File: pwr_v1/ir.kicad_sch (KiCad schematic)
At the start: 1 part

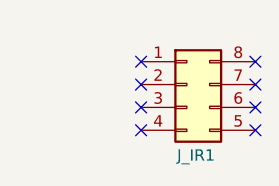
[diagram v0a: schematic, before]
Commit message: Sch and Layout updated; Added batt sup ckt, placed and routed all motor drivers.
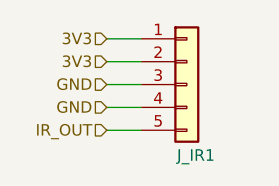
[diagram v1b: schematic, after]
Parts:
- J_IR1: value Conn_02x04_Counter_Clockwise -> Connector_Generic:Conn_01x05; symbol Connector_Generic:Conn_02x04_Counter_Clockwise -> Connector_Generic:Conn_01x05
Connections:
- net 3V3: now reaches J_IR1.1 (Pin_1)
- net 3V3: now also J_IR1.2 (Pin_2)
- net GND: now reaches J_IR1.3 (Pin_3)
- net GND: now also J_IR1.4 (Pin_4)
- net IR_OUT: now reaches J_IR1.5 (Pin_5)
- no-connect marks 8 -> 0
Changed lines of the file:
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@@
 	(generator_version "8.0")
 	(paper "A5")
-	(no_connect
-		(at 92.71 66.04)
+	(wire
+		(pts
+			(xy 88.9 60.96) (xy 92.71 60.96)
+		)
+		(stroke
+			(width 0)
+			(type default)
+		)
 	)
-	(no_connect
-		(at 105.41 58.42)
+	(wire
+		(pts
+			(xy 88.9 63.5) (xy 92.71 63.5)
+		)
+		(stroke
+			(width 0)
+			(type default)
+		)
 	)
-	(no_connect
-		(at 105.41 66.04)
+	(wire
+		(pts
+			(xy 88.9 58.42) (xy 92.71 58.42)
+		)
+		(stroke
+			(width 0)
+			(type default)
+		)
 	)
-	(no_connect
-		(at 92.71 58.42)
+	(wire
+		(pts
+			(xy 88.9 66.04) (xy 92.71 66.04)
+		)
+		(stroke
+			(width 0)
+			(type default)
+		)
 	)
-	(no_connect
-		(at 105.41 63.5)
+	(wire
+		(pts
+			(xy 88.9 55.88) (xy 92.71 55.88)
+		)
+		(stroke
+			(width 0)
+			(type default)
+		)
 	)
-	(no_connect
-		(at 92.71 63.5)
+	(hierarchical_label "GND"
+		(shape input)
+		(at 88.9 63.5 180)
+		(fields_autoplaced yes)
+		(effects
+			(font
+				(size 1.27 1.27)
+			)
+			(justify right)
+		)
 	)
-	(no_connect
-		(at 92.71 60.96)
+	(hierarchical_label "3V3"
+		(shape input)
+		(at 88.9 55.88 180)
+		(fields_autoplaced yes)
+		(effects
+			(font
+				(size 1.27 1.27)
+			)
+			(justify right)
+		)
 	)
-	(no_connect
-		(at 105.41 60.96)
+	(hierarchical_label "IR_OUT"
+		(shape input)
+		(at 88.9 66.04 180)
+		(fields_autoplaced yes)
+		(effects
+			(font
+				(size 1.27 1.27)
+			)
+			(justify right)
+		)
+	)
+	(hierarchical_label "3V3"
+		(shape input)
+		(at 88.9 58.42 180)
+		(fields_autoplaced yes)
+		(effects
+			(font
+				(size 1.27 1.27)
+			)
+			(justify right)
+		)
+	)
+	(hierarchical_label "GND"
+		(shape input)
+		(at 88.9 60.96 180)
+		(fields_autoplaced yes)
+		(effects
+			(font
+				(size 1.27 1.27)
+			)
+			(justify right)
+		)
 	)
 	(symbol
-		(lib_id "Connector_Generic:Conn_02x04_Counter_Clockwise")
+		(lib_id "Connector_Generic:Conn_01x05")
 		(at 97.79 60.96 0)
 		(unit 1)
@@
 			)
 		)
-		(property "Value" "Conn_02x04_Counter_Clockwise"
+		(property "Value" "Connector_Generic:Conn_01x05"
 			(at 99.06 54.61 0)
 			(effects
@@
 			)
 		)
-		(property "Description" "Generic connector, double row, 02x04, counter clockwise pin numbering scheme (similar to DIP package numbering), script generated (kicad-library-utils/schlib/autogen/connector/)"
+		(property "Description" "Generic connector, single row, 01x05, script generated (kicad-library-utils/schlib/autogen/connector/)"
 			(at 97.79 60.96 0)
 			(effects
@@
 		(pin "3"
 		)
-		(pin "6"
-		)
 		(pin "4"
 		)
@@
 		(pin "1"
 		)
-		(pin "7"
-		)
-		(pin "8"
-		)
 		(instances

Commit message: Schematic and layout updated; Motor driver alignments and planes;  Few components updated
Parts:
- J_IR1: footprint (none) -> Connector_PinHeader_2.54mm:PinHeader_1x05_P2.54mm_Vertical
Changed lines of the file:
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@@
 			)
 		)
-		(property "Footprint" ""
+		(property "Footprint" "Connector_PinHeader_2.54mm:PinHeader_1x05_P2.54mm_Vertical"
 			(at 97.79 60.96 0)
 			(effects
@@
 			)
 		)
-		(property "Description" "Generic connector, single row, 01x05, script generated (kicad-library-utils/schlib/autogen/connector/)"
+		(property "Description" ""
 			(at 97.79 60.96 0)
 			(effects

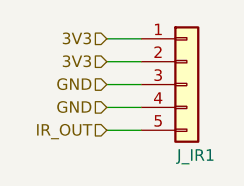
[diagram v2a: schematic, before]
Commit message: Schematic updated; Layout updated; STM PinMappings file added
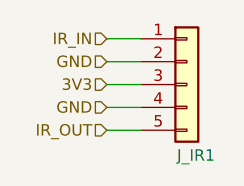
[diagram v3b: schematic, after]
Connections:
- net 3V3: now also J_IR1.3 (Pin_3); no longer J_IR1.1 (Pin_1), J_IR1.2 (Pin_2)
- net GND: now also J_IR1.2 (Pin_2); no longer J_IR1.3 (Pin_3)
- new net IR_IN: J_IR1.1 (Pin_1)
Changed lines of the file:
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@@
 		)
 	)
-	(hierarchical_label "3V3"
+	(hierarchical_label "IR_IN"
 		(shape input)
 		(at 88.9 55.88 180)
@@
 		)
 	)
-	(hierarchical_label "3V3"
+	(hierarchical_label "GND"
 		(shape input)
 		(at 88.9 58.42 180)
@@
 		)
 	)
-	(hierarchical_label "GND"
+	(hierarchical_label "3V3"
 		(shape input)
 		(at 88.9 60.96 180)

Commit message: Schematic and layout updated; Layout placement and routing completed
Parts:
- J_IR1: footprint Connector_PinHeader_2.54mm:PinHeader_1x05_P2.54mm_Vertical -> Connector_PinHeader_2.54mm:PinHeader_1x05_P2.54mm_Vertical_SMD_Pin1Left
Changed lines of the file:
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@@
 			)
 		)
-		(property "Footprint" "Connector_PinHeader_2.54mm:PinHeader_1x05_P2.54mm_Vertical"
+		(property "Footprint" "Connector_PinHeader_2.54mm:PinHeader_1x05_P2.54mm_Vertical_SMD_Pin1Left"
 			(at 97.79 60.96 0)
 			(effects

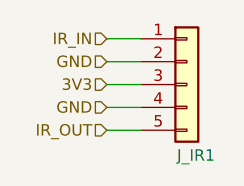
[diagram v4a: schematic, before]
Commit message: Sch: DNP updated, JLC part numbers updated for all components; Lay: Fiducial placement, routing aligned.
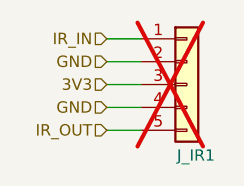
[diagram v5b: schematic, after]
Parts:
- J_IR1: now not fitted; now left out of the parts list
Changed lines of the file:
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@@
 		(unit 1)
 		(exclude_from_sim no)
-		(in_bom yes)
+		(in_bom no)
 		(on_board yes)
-		(dnp no)
+		(dnp yes)
 		(property "Reference" "J_IR1"
 			(at 98.806 68.834 0)

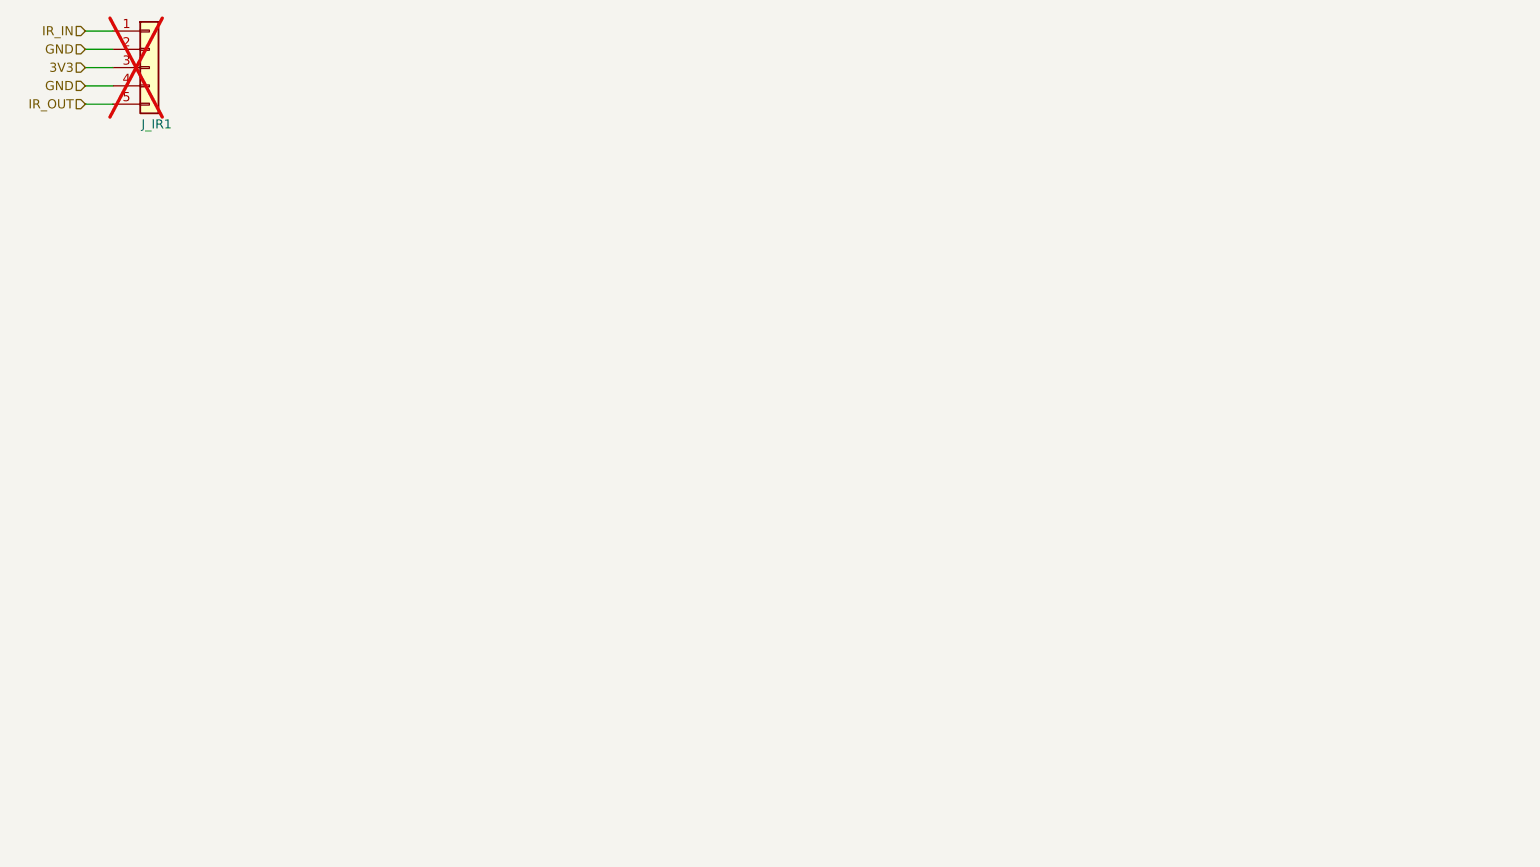
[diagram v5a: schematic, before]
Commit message: File structure enhanced.
Added uniform titleblocks and 3D renders for easier view, file cleanups.
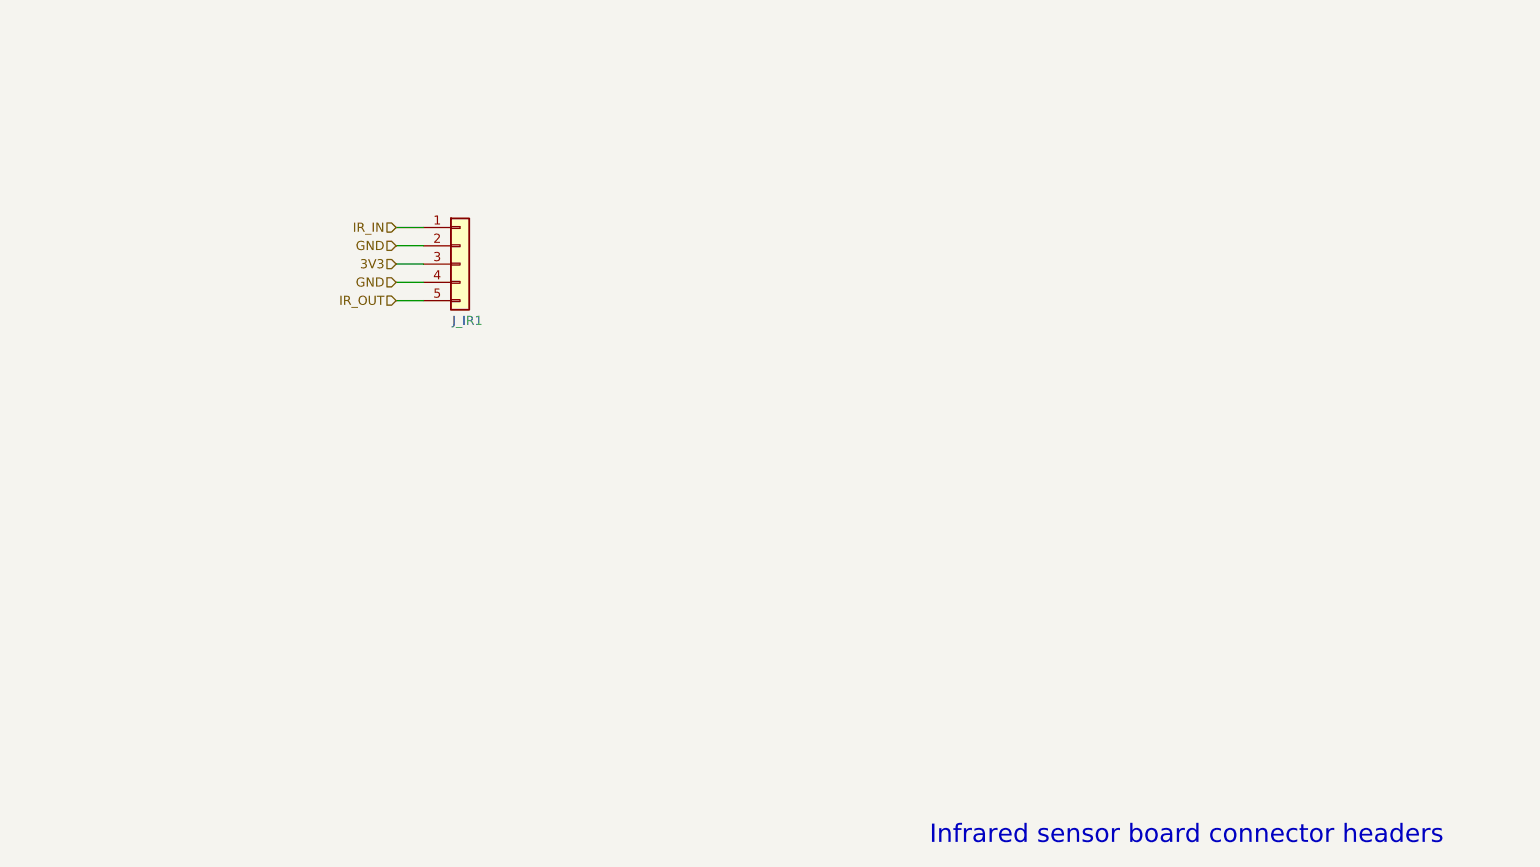
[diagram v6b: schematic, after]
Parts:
- J_IR1: now fitted
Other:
- note added: "Infrared sensor board connector headers"
- title: (none) -> Power board
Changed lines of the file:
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@@
 (kicad_sch
-	(version 20231120)
+	(version 20250114)
 	(generator "eeschema")
-	(generator_version "8.0")
-	(paper "A5")
+	(generator_version "9.0")
+	(paper "A4")
+	(title_block
+		(title "Power board")
+		(date "06-08-2024")
+		(rev "1")
+	)
+	(text "Infrared sensor board connector headers"
+		(exclude_from_sim no)
+		(at 241.935 167.64 0)
+		(effects
+			(font
+				(face "Gidole")
+				(size 2.54 2.54)
+			)
+		)
+	)
 	(wire
 		(pts
-			(xy 88.9 60.96) (xy 92.71 60.96)
+			(xy 132.08 88.265) (xy 135.89 88.265)
 		)
 		(stroke
@@
 	(wire
 		(pts
-			(xy 88.9 63.5) (xy 92.71 63.5)
+			(xy 132.08 90.805) (xy 135.89 90.805)
 		)
 		(stroke
@@
 	(wire
 		(pts
-			(xy 88.9 58.42) (xy 92.71 58.42)
+			(xy 132.08 85.725) (xy 135.89 85.725)
 		)
 		(stroke
@@
 	(wire
 		(pts
-			(xy 88.9 66.04) (xy 92.71 66.04)
+			(xy 132.08 93.345) (xy 135.89 93.345)
 		)
 		(stroke
@@
 	(wire
 		(pts
-			(xy 88.9 55.88) (xy 92.71 55.88)
+			(xy 132.08 83.185) (xy 135.89 83.185)
 		)
 		(stroke
@@
 	(hierarchical_label "GND"
 		(shape input)
-		(at 88.9 63.5 180)
-		(fields_autoplaced yes)
+		(at 132.08 90.805 180)
 		(effects
 			(font
@@
 	(hierarchical_label "IR_IN"
 		(shape input)
-		(at 88.9 55.88 180)
-		(fields_autoplaced yes)
+		(at 132.08 83.185 180)
 		(effects
 			(font
@@
 	(hierarchical_label "IR_OUT"
 		(shape input)
-		(at 88.9 66.04 180)
-		(fields_autoplaced yes)
+		(at 132.08 93.345 180)
 		(effects
 			(font
@@
 	(hierarchical_label "GND"
 		(shape input)
-		(at 88.9 58.42 180)
-		(fields_autoplaced yes)
+		(at 132.08 85.725 180)
 		(effects
 			(font
@@
 	(hierarchical_label "3V3"
 		(shape input)
-		(at 88.9 60.96 180)
-		(fields_autoplaced yes)
+		(at 132.08 88.265 180)
 		(effects
 			(font
@@
 	(symbol
 		(lib_id "Connector_Generic:Conn_01x05")
-		(at 97.79 60.96 0)
+		(at 140.97 88.265 0)
 		(unit 1)
 		(exclude_from_sim no)
 		(in_bom no)
 		(on_board yes)
-		(dnp yes)
+		(dnp no)
 		(property "Reference" "J_IR1"
-			(at 98.806 68.834 0)
+			(at 141.986 96.139 0)
 			(effects
 				(font
@@
 		)
 		(property "Value" "Connector_Generic:Conn_01x05"
-			(at 99.06 54.61 0)
+			(at 142.24 81.915 0)
 			(effects
 				(font
@@
 		)
 		(property "Footprint" "Connector_PinHeader_2.54mm:PinHeader_1x05_P2.54mm_Vertical_SMD_Pin1Left"
-			(at 97.79 60.96 0)
+			(at 140.97 88.265 0)
 			(effects
 				(font
@@
 		)
 		(property "Datasheet" "~"
-			(at 97.79 60.96 0)
+			(at 140.97 88.265 0)
 			(effects
 				(font
@@
 		)
 		(property "Description" ""
-			(at 97.79 60.96 0)
+			(at 140.97 88.265 0)
 			(effects
 				(font
